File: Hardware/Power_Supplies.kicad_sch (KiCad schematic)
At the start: 10 parts, among them U3 LM1086-ADJ, U4 LM1086-ADJ

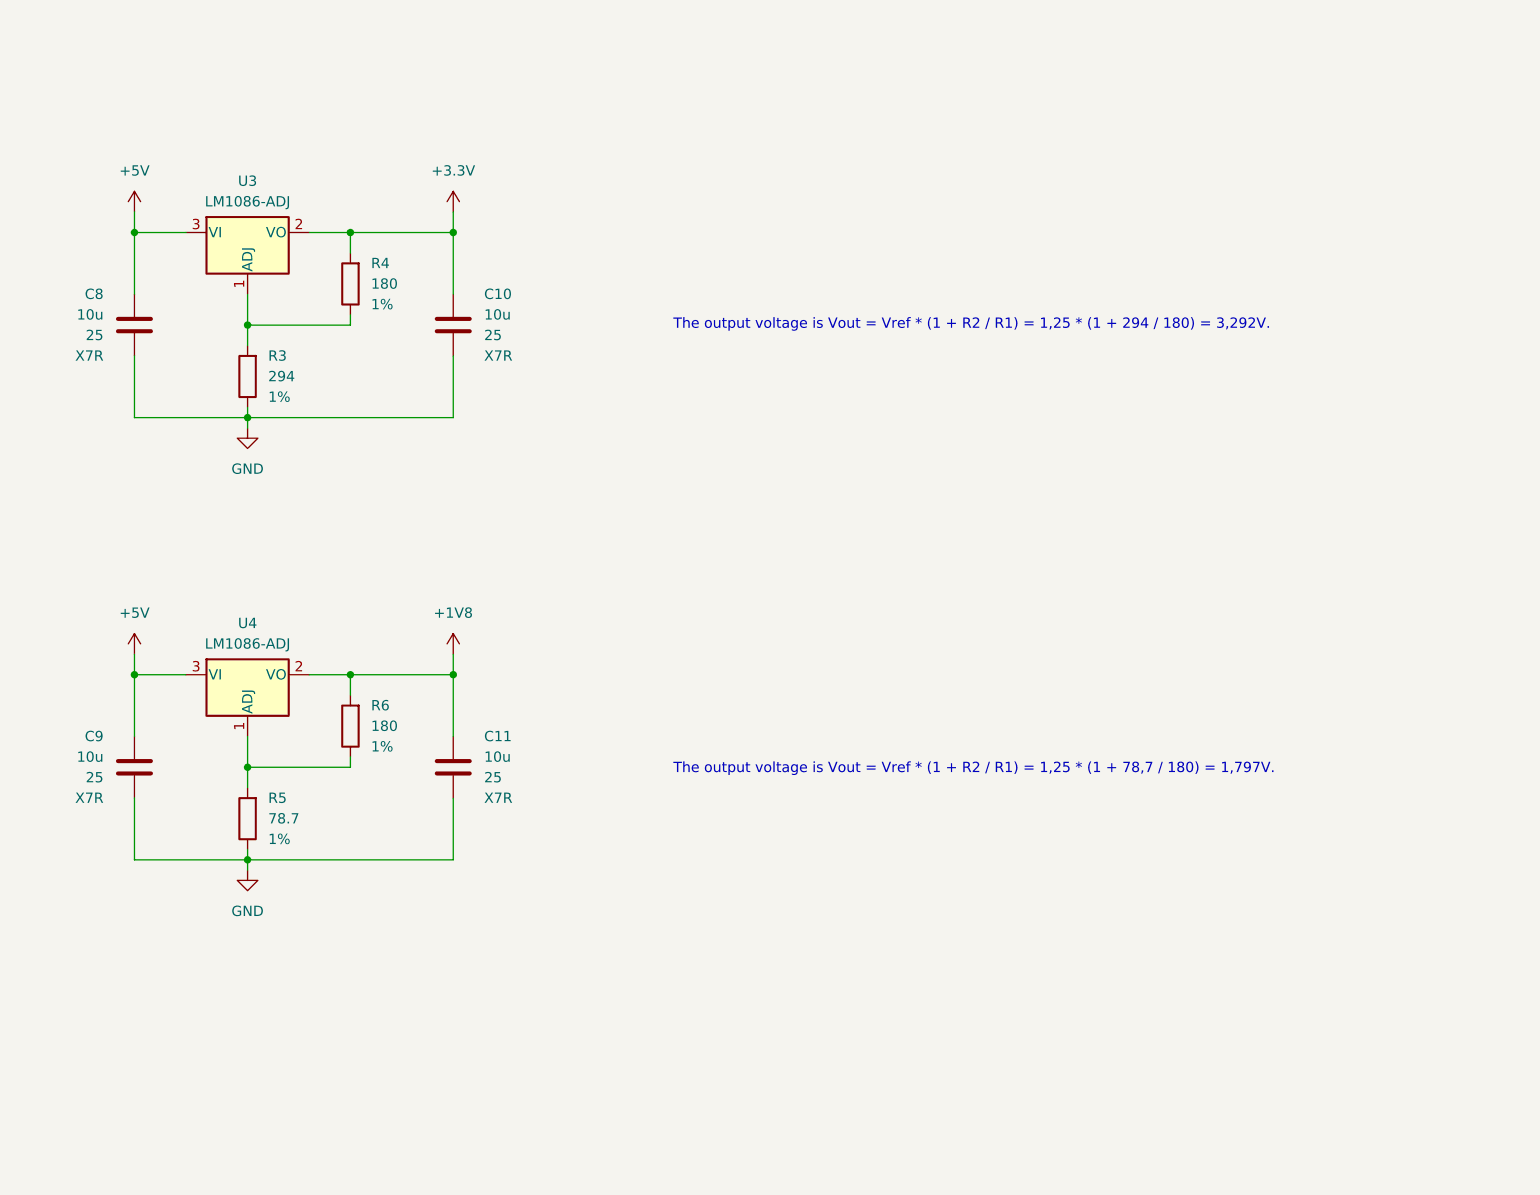
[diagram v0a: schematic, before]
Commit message: [Hardware] Added a pin header connector to provide the output power supply.
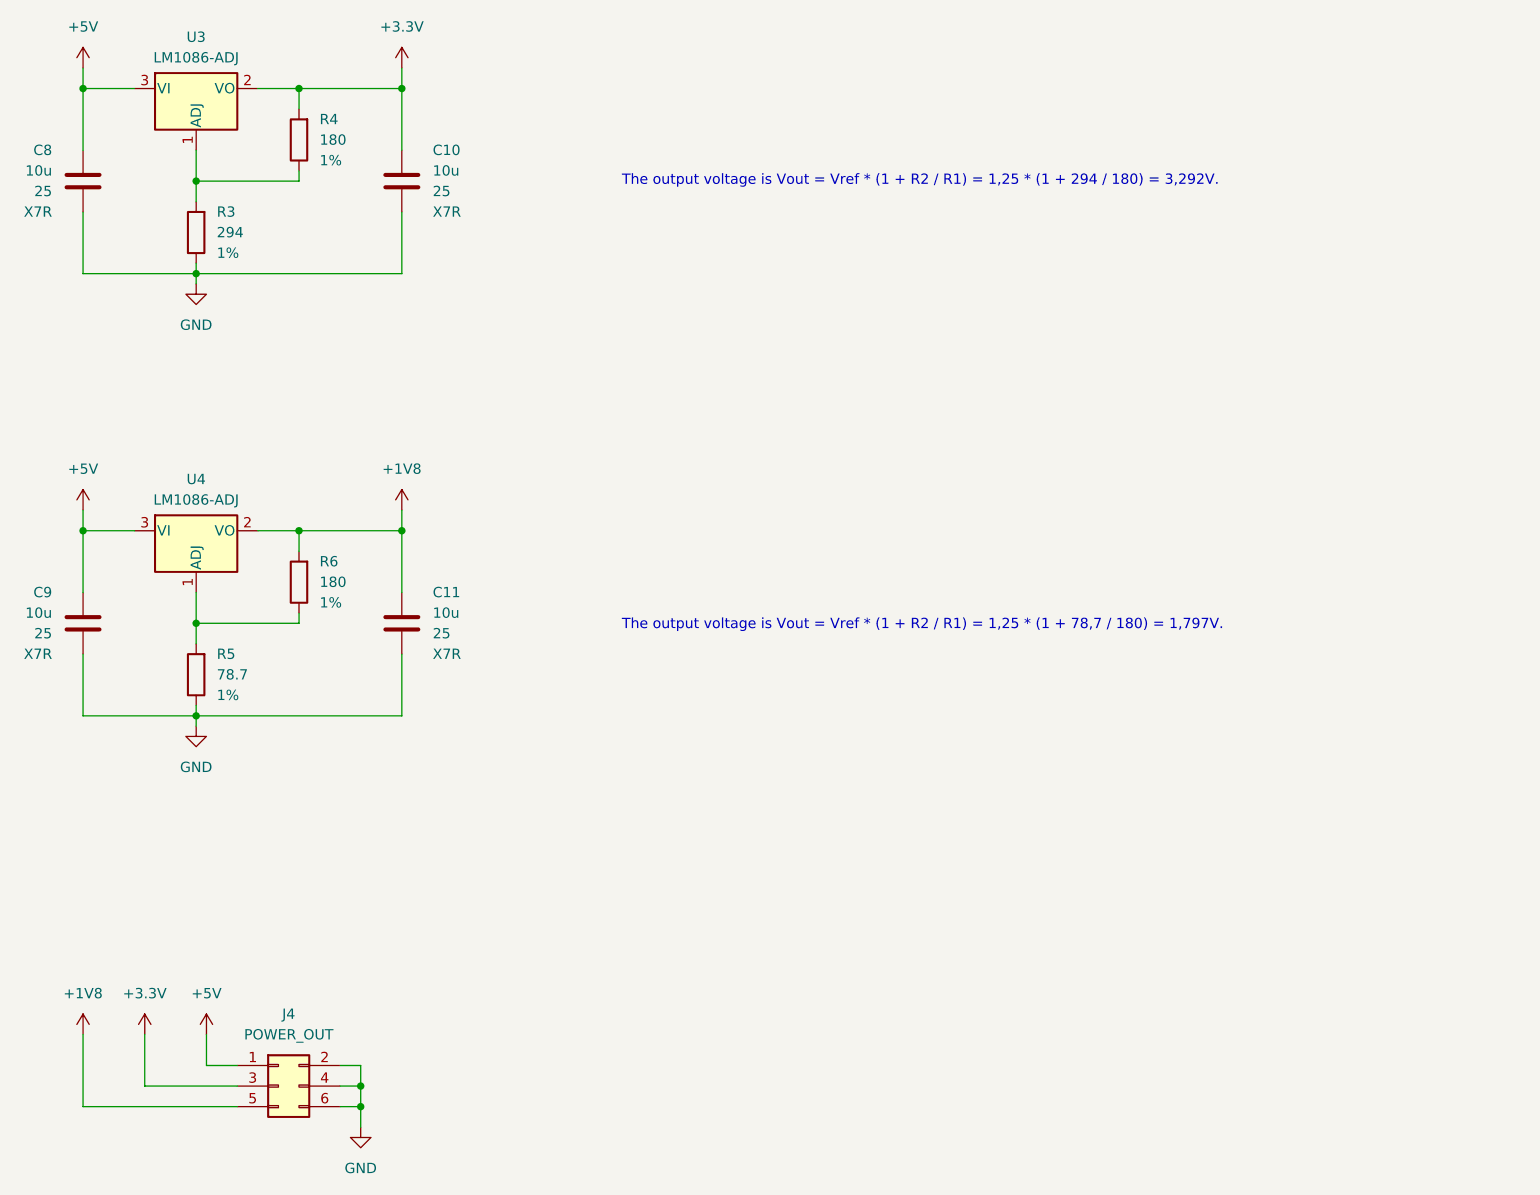
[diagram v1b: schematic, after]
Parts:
- added J4: POWER_OUT, Connector_PinHeader_2.54mm:PinHeader_2x03_P2.54mm_Horizontal, symbol Connector_Generic:Conn_02x03_Odd_Even
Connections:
- net +1V8: now also J4.5 (Pin_5)
- net +3.3V: now also J4.3 (Pin_3)
- net +5V: now also J4.1 (Pin_1)
- net GND: now also J4.2 (Pin_2), J4.4 (Pin_4), J4.6 (Pin_6)
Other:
- moved on the sheet: C10, C11, C8, C9, R3, R4, R5, R6, U3, U4

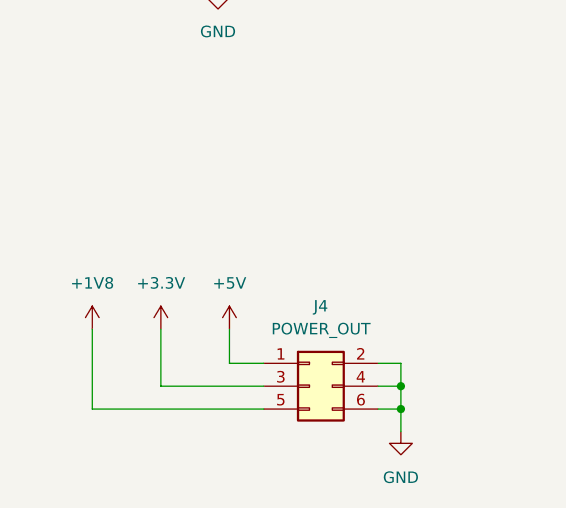
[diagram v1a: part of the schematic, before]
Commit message: [Hardware] Routed the voltage regulators.
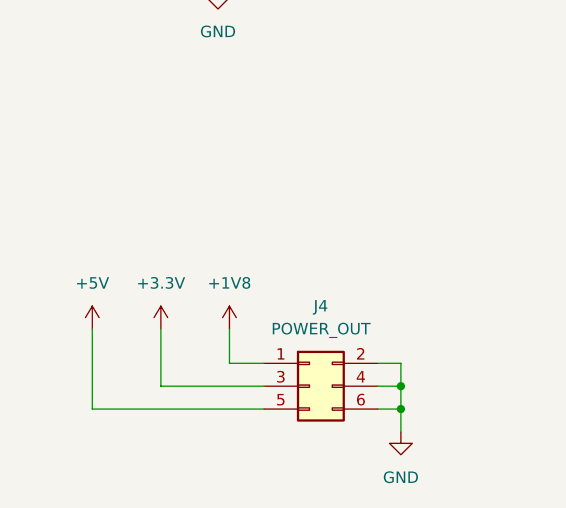
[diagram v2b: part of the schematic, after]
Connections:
- net +1V8: now also J4.1 (Pin_1); no longer J4.5 (Pin_5)
- net +5V: now also J4.5 (Pin_5); no longer J4.1 (Pin_1)

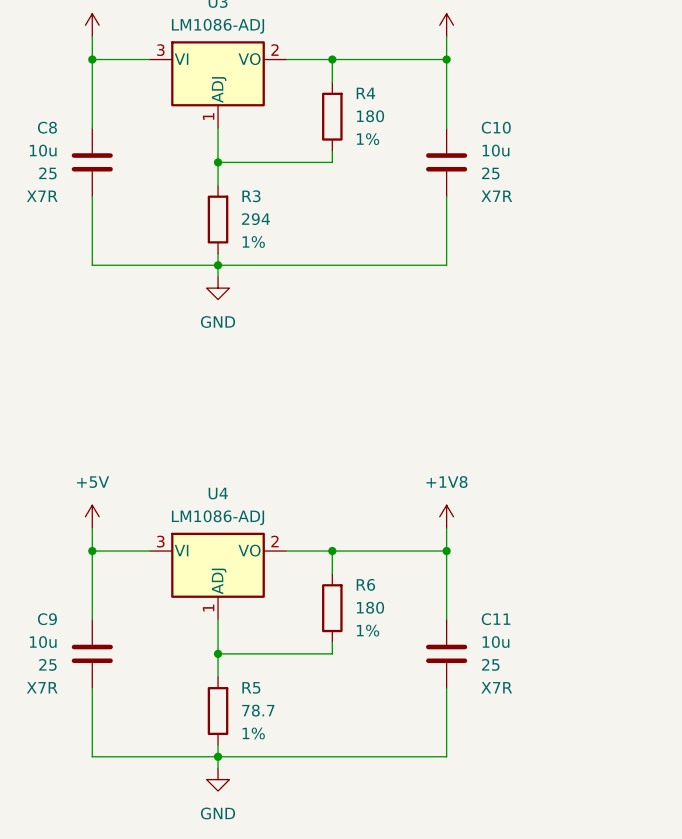
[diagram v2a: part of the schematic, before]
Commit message: [Hardware] Also grouped the components per value 2 and 3 fields when exporting the bill of materials.
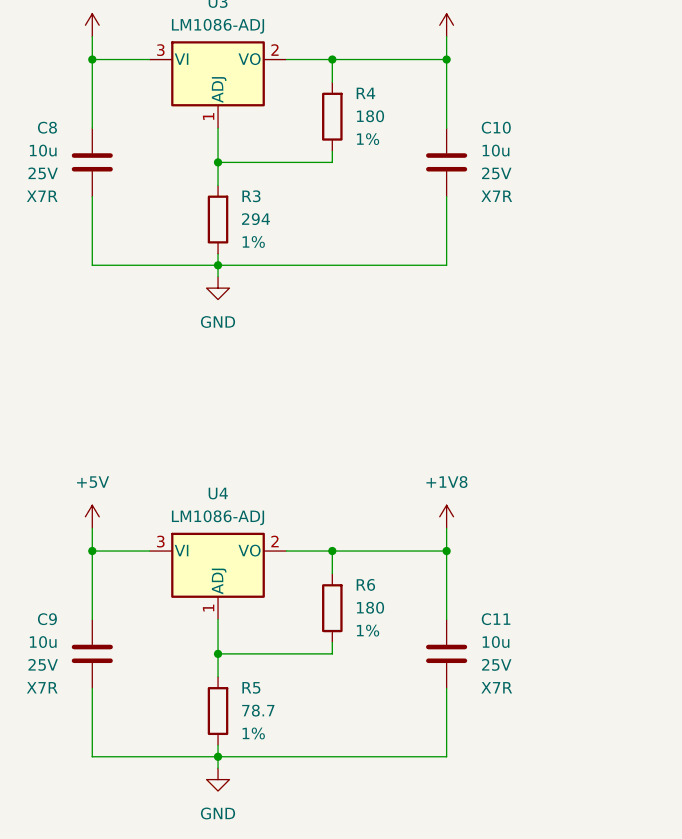
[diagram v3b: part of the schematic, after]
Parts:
- C10, C11, C8, C9: Value2 25 -> 25V
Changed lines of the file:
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@@
 			)
 		)
-		(property "Value2" "25"
+		(property "Value2" "25V"
 			(at 119.38 100.3299 0)
 			(effects
@@
 			)
 		)
-		(property "Value2" "25"
+		(property "Value2" "25V"
 			(at 72.39 100.3299 0)
 			(effects
@@
 			)
 		)
-		(property "Value2" "25"
+		(property "Value2" "25V"
 			(at 119.38 45.7199 0)
 			(effects
@@
 			)
 		)
-		(property "Value2" "25"
+		(property "Value2" "25V"
 			(at 72.39 45.7199 0)
 			(effects
